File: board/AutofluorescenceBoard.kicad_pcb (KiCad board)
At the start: 4 copper layers, 44.4 x 44.5 mm, 40 parts, among them J1 2002411212, Q1 BSS138, U1 PAM2863ECR, U2 PAM2863ECR, U3 PAM2863ECR

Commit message: Some Board Review Changes
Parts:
- Conn1: footprint AutofluorescenceBoard:MOLEX_SL_05_Vertical_AF -> MRDT_Connectors:MOLEX_SL_05_Horizontal
- D3: value 490nm -> 500nm
- D6: value LED -> WHT LED
- FanConn1: footprint AutofluorescenceBoard:MOLEX_SL_02_Horizontal -> MRDT_Connectors:MOLEX_SL_02_Horizontal
- J1: footprint AutofluorescenceBoard:CONN_SD-172286-1000_02_MOL -> MRDT_Connectors:MOLEX_SL_02_Horizontal
- moved Conn1 1.02 mm to (134.6, 64.0)
- moved J1 0.83 mm to (151.4, 64.0)
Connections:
- FanConn1 pad 1: +12V -> GND
- FanConn1 pad 2: GND -> +12V
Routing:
- net ISET 490nm: track 87.0 -> 52.5 mm, vias 3 -> 2
- net Net-(CR2-Pad2): track 53.1 -> 34.5 mm, vias 4 -> 3
- net +12V: track 0.00 -> 12.4 mm, vias 19 -> 18
- net Net-(D3-Pad1): track 34.1 -> 25.4 mm
- net Net-(U2-ISENSE): track 22.1 -> 14.4 mm, vias 3 -> 2
- net ISET 405nm: track 35.2 -> 28.1 mm, vias 3 -> 1
- net Net-(D4-A): track 21.9 -> 15.6 mm
- net Net-(D3-Pad2): track 4.68 -> 9.30 mm
- net Net-(J1-Pad2): track 10.2 -> 11.4 mm, vias 5 -> 0
- net White LED: track 9.60 -> 10.6 mm, vias 3 -> 0
- net Net-(U3-ISENSE): track 11.2 -> 12.2 mm, vias 3 -> 0
- net ISET 365nm: track 37.1 -> 38.0 mm, vias 3 -> 1
- net Net-(D1-Pad2): track 9.30 -> 9.98 mm, vias 2 -> 1
- net Net-(D1-Pad1): track 16.4 -> 15.8 mm
- net Net-(CR3-Pad2): vias 4 -> 0
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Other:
- board text added: "500"
- board text removed: "490"

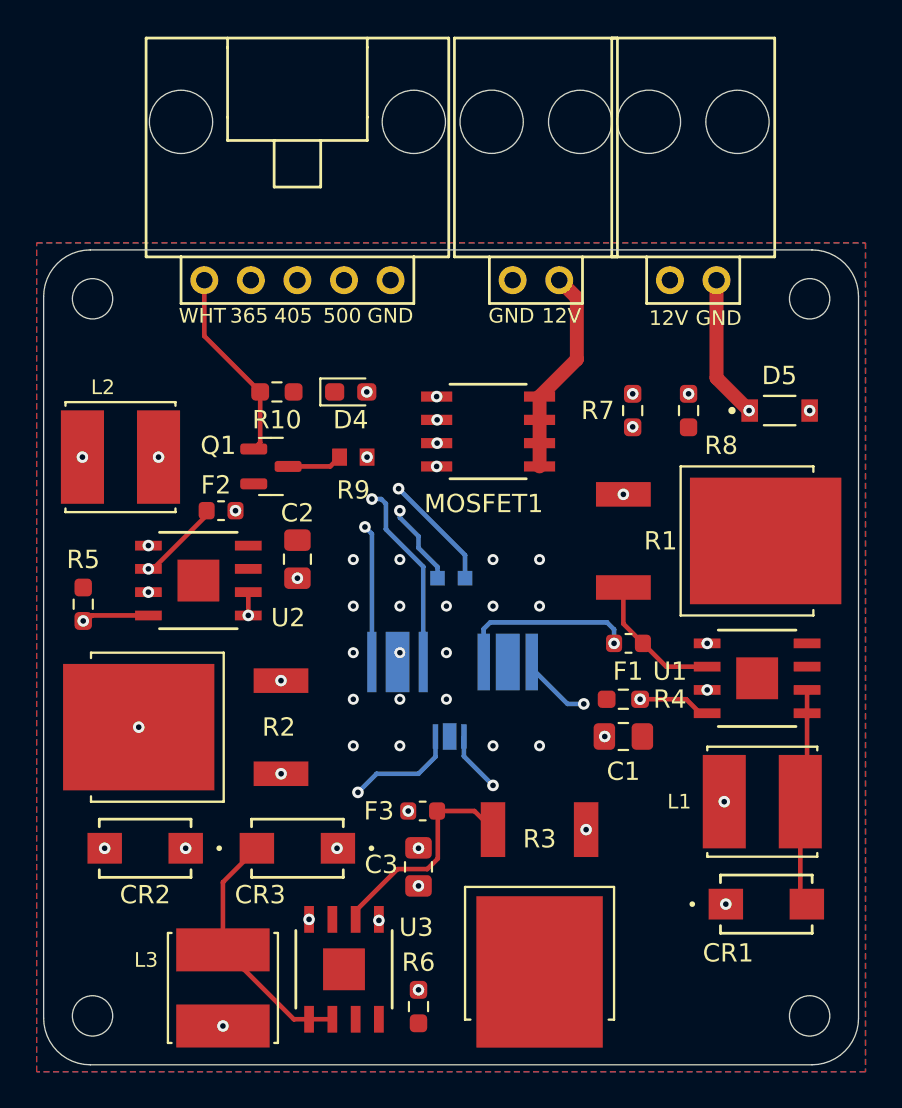
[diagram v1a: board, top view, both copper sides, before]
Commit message: Screwed Up MRDT Library on Laptop
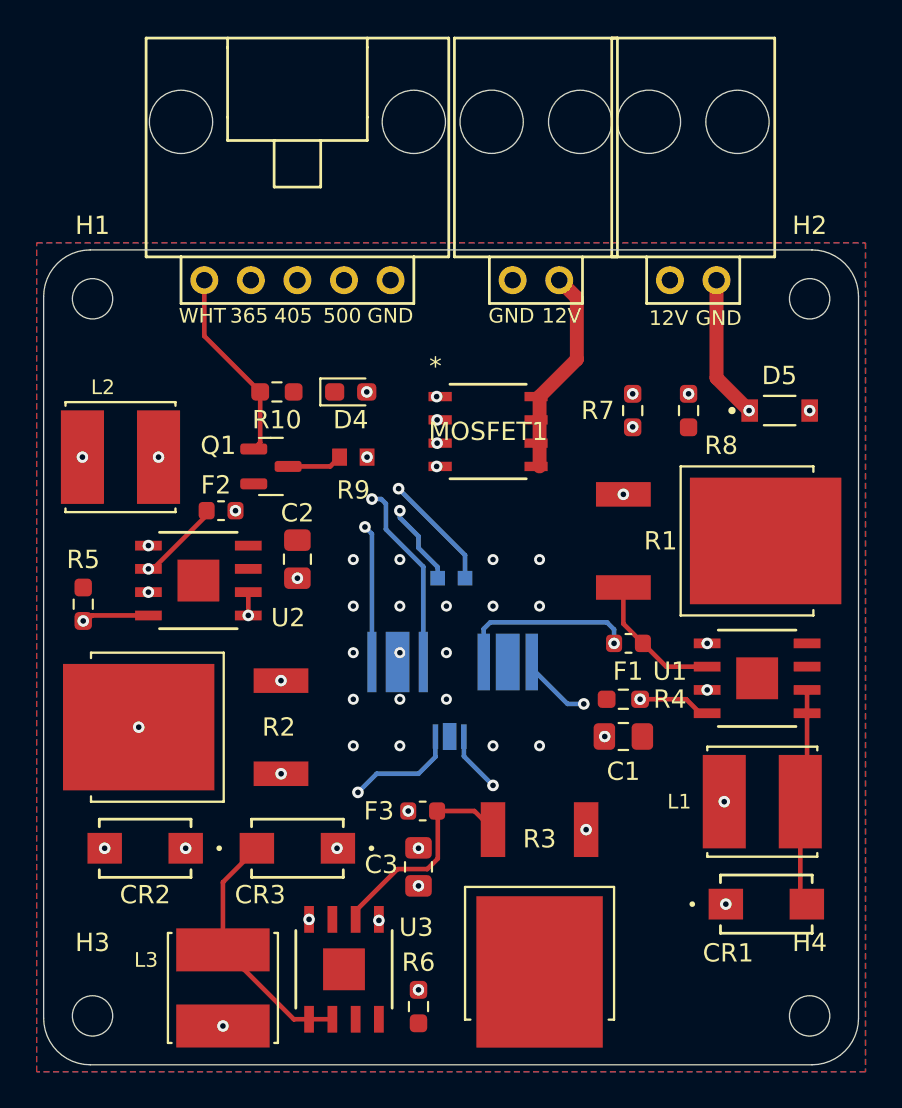
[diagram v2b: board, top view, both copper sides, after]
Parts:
- D3: value 500nm -> 490nm
- D6: value WHT LED -> LED
- H1, H2, H3, H4: footprint MountingHole:MountingHole_2.2mm_M2 -> MRDT_Drill_Holes:M2_Hole
- MOSFET1: footprint AutofluorescenceBoard:SOP-8_TOS-M -> MRDT_Devices:SOP-8_TOS-L
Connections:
- FanConn1 pad 1: GND -> +12V
- FanConn1 pad 2: +12V -> GND

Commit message: Updated Schematic, Mounting Holes, and a couple 3D models
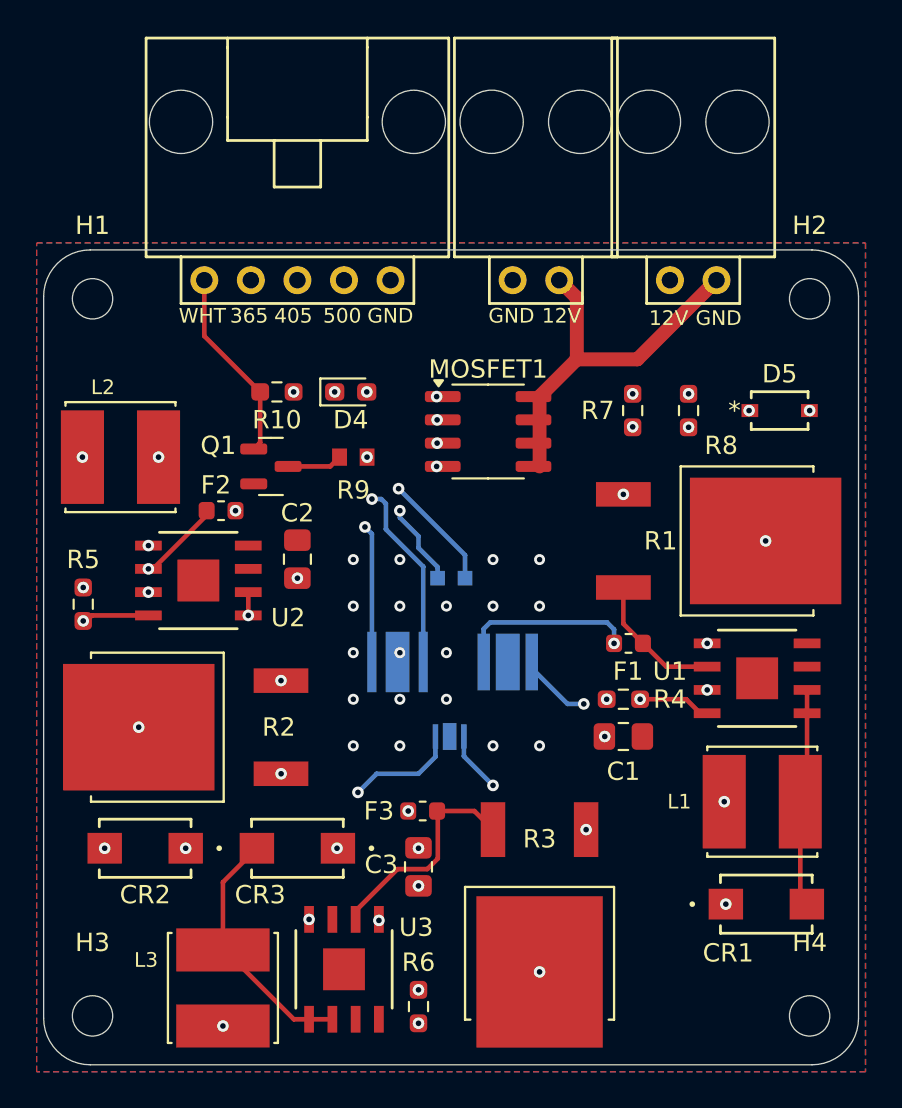
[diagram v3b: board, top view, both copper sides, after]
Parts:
- D3: value 490nm -> 500nm
- D5: footprint AutofluorescenceBoard:DIO_MMSZ5221BT1G -> MRDT_Devices:SOD-123_ONS-L
- MOSFET1: footprint MRDT_Devices:SOP-8_TOS-L -> Package_SO:SOIC-8_3.9x4.9mm_P1.27mm
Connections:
- FanConn1 pad 1: +12V -> GND
- FanConn1 pad 2: GND -> Net-(MOSFET1-D)
- J1 pad 2: Net-(J1-Pad2) -> Net-(MOSFET1-D)
- MOSFET1 pad 5: Net-(J1-Pad2) -> Net-(MOSFET1-D)
- MOSFET1 pad 6: Net-(J1-Pad2) -> Net-(MOSFET1-D)
- MOSFET1 pad 7: Net-(J1-Pad2) -> Net-(MOSFET1-D)
- MOSFET1 pad 8: Net-(J1-Pad2) -> Net-(MOSFET1-D)
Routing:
- net Net-(MOSFET1-D): track 0.00 -> 20.8 mm
- net Net-(J1-Pad2): track 11.4 -> 0.00 mm
- net +12V: track 12.4 -> 4.53 mm
- net GND: vias 23 -> 31

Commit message: Fixed white led silkscreen
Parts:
- D6: value LED -> WHT LED
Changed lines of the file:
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@@
 		)
 		(fp_text user "${REFERENCE}"
-			(at 3.08 0.93 0)
+			(at 4.8595 0.016 0)
 			(unlocked yes)
 			(layer "B.SilkS")
@@
 			)
 		)
-		(property "Value" "LED"
-			(at -0.369 2.794 0)
+		(property "Value" "WHT LED"
+			(at -0.242 2.667 0)
 			(layer "B.SilkS")
 			(effects
@@
 		(sheetfile "AutofluorescenceBoard.kicad_sch")
 		(attr smd)
-		(fp_circle
-			(center 1.72 -0.01)
-			(end 1.72 -0.02)
-			(stroke
-				(width 0.1)
-				(type default)
-			)
-			(fill no)
-			(layer "B.SilkS")
-		)
 		(fp_line
 			(start 2.15 1.4)

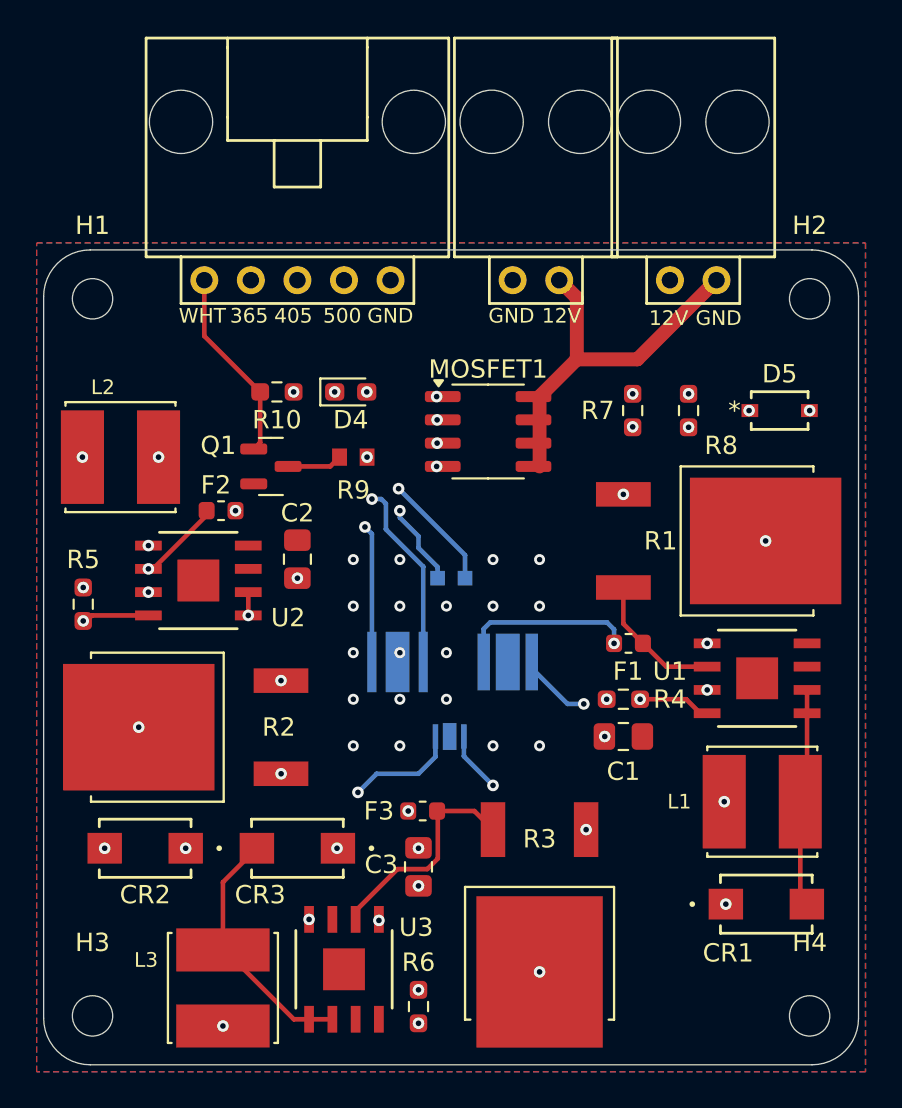
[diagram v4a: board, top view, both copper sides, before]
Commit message: Added 3D models and some silkscreen
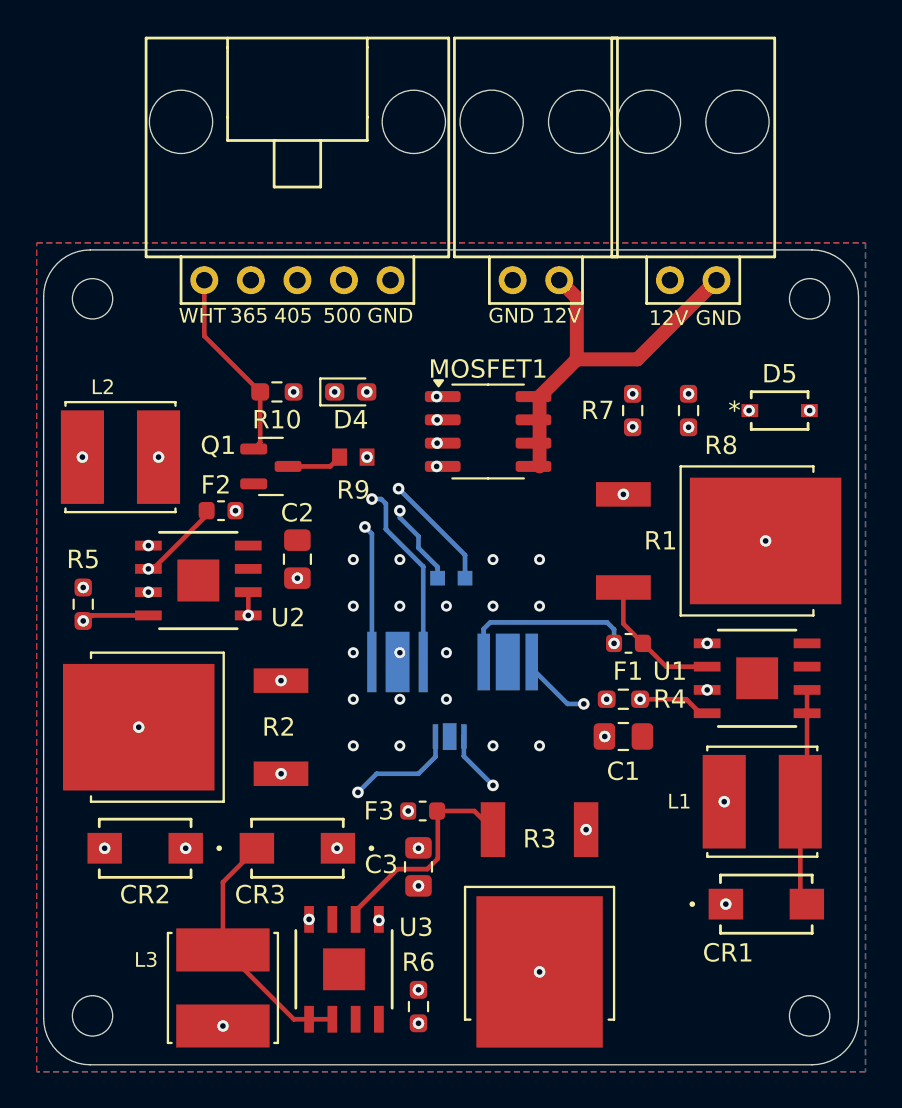
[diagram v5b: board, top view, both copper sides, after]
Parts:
- added G***: LOGO, LOGO, B.Cu at (166.2, 73.0)
- added G***: LOGO, MRDT_Silkscreens:0-README, B.Cu at (150.0, 102.9)
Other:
- board text added: "Autofluorescence Board Rev2"
- board text added: "Mars Rover Design Team"
- board text added: "Missouri S&T, 2026"
- board text added: "Mitchell Hocking"

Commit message: Added GND Thermal stuff on power plane
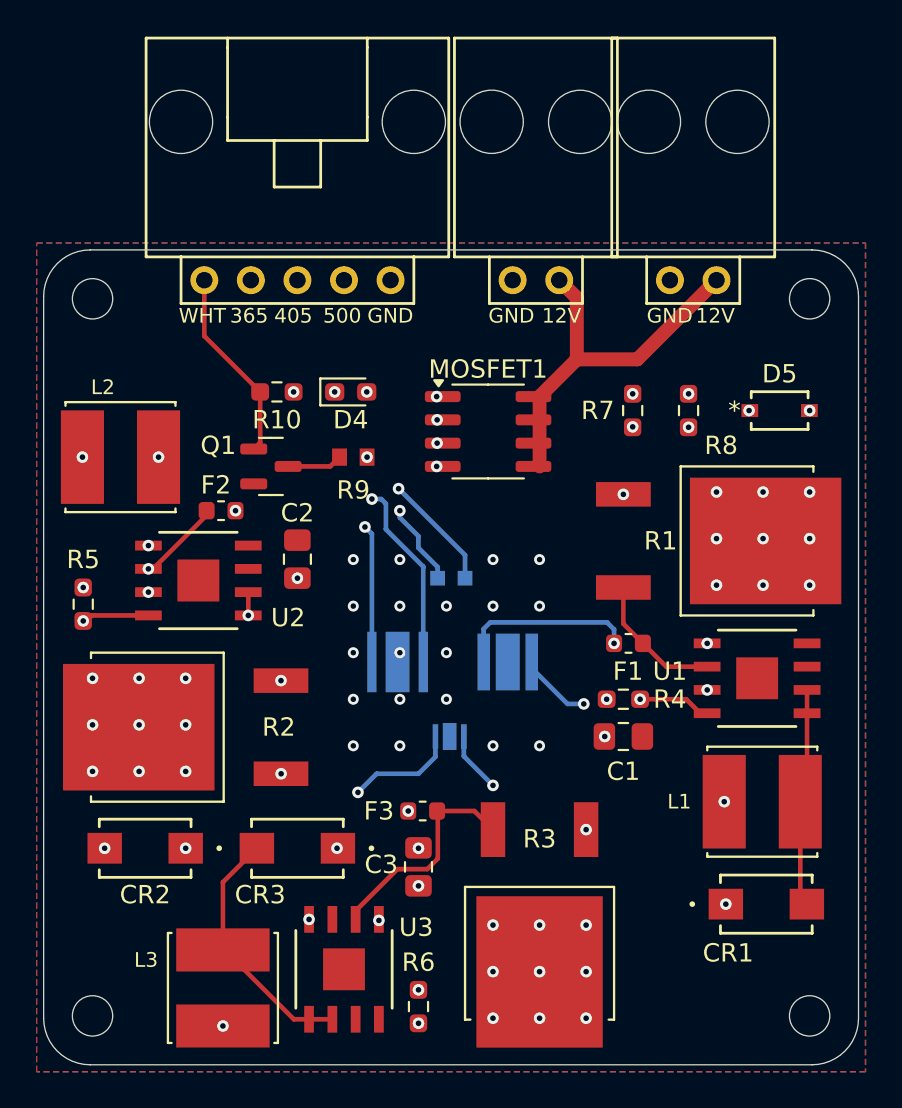
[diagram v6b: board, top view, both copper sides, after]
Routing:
- net ISET 490nm: track 52.5 -> 63.3 mm
- net ISET 365nm: track 38.0 -> 37.5 mm
- net GND: vias 31 -> 55
- added copper zone on In1.Cu, net GND

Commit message: Added Signature
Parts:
- added G***: LOGO, LOGO, B.Cu at (155.4, 105.0)
- moved G*** 1.91 mm to (150.1, 101.0)

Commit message: VIAS
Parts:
- moved G*** 4.60 mm to (163.3, 76.6)
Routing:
- net GND: vias 55 -> 67
- net (no net): vias 0 -> 24
